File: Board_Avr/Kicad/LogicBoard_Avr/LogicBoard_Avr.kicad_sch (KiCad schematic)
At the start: 4 parts

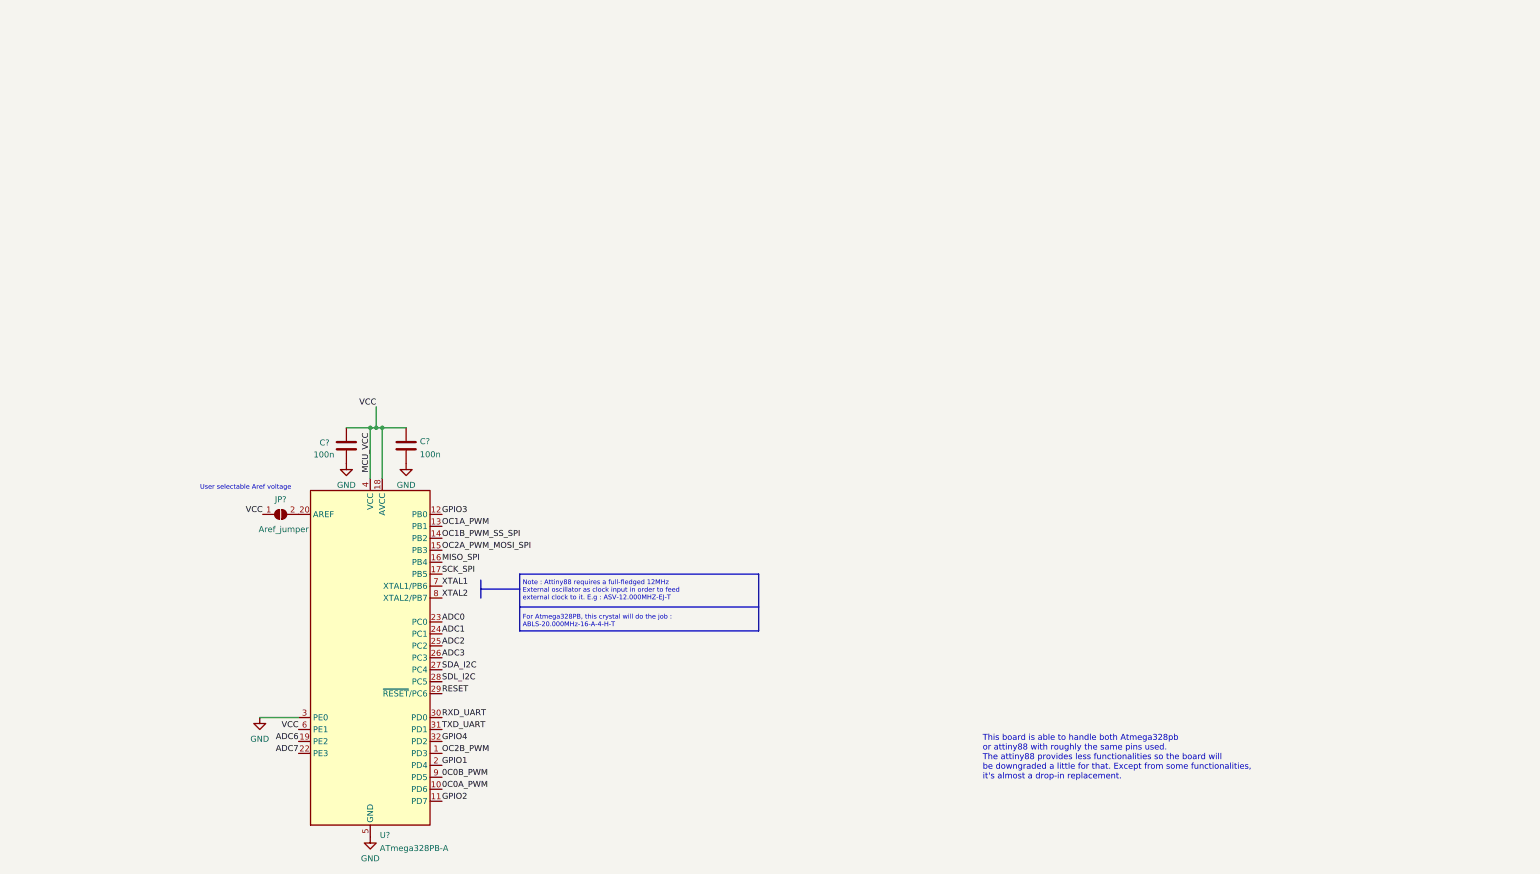
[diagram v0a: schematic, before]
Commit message: Added the Mechanical user interface hierarchical sheet and started schematics
Signed-off-by: bebenlebricolo <benoittarrade@hotmail.fr>
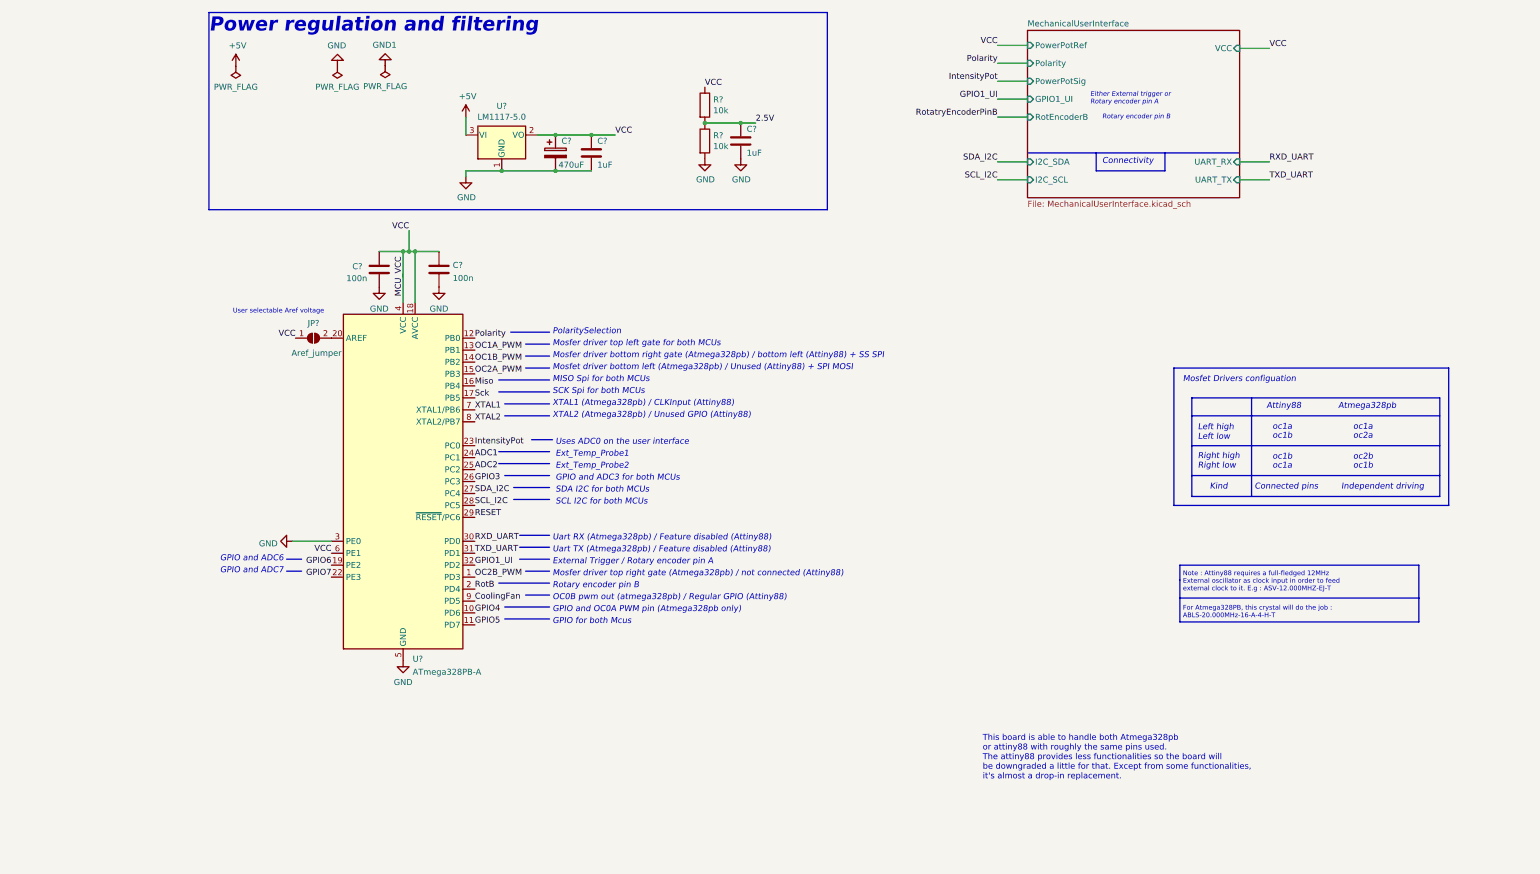
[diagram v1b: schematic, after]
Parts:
- added C? (x2): 1uF, Capacitor_SMD:C_1206_3216Metric_Pad1.33x1.80mm_HandSolder, symbol Device:C
- added C?: 470uF, Capacitor_SMD:CP_Elec_10x10, symbol Device:CP
- added R? (x2): 10k, Resistor_SMD:R_1206_3216Metric_Pad1.30x1.75mm_HandSolder, symbol Device:R
- added U?: LM1117-5.0, Package_TO_SOT_SMD:SOT-223-3_TabPin2, symbol Regulator_Linear:LM1117-5.0
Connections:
- net 0C0A_PWM is gone; now on net GPIO4: U?.10 (PD6)
- net ADC3 is gone; now on net GPIO3: U?.26 (PC3)
- net GND: now also C?.2, C?.2, C?.2, R?.2, U?.1 (GND)
- net GPIO3: no longer U?.12 (PB0)
- net GPIO4: no longer U?.32 (PD2)
- net MCU_VCC: now also C?.1, C?.1, R?.1, U?.2 (VO)
- net 0C0B_PWM renamed CoolingFan
- net ADC0 renamed IntensityPot
- net ADC6 renamed GPIO6
- net ADC7 renamed GPIO7
- net GPIO1 renamed RotB
- net GPIO2 renamed GPIO5
- net MISO_SPI renamed Miso
- net OC1B_PWM_SS_SPI renamed OC1B_PWM
- net OC2A_PWM_MOSI_SPI renamed OC2A_PWM
- net SCK_SPI renamed Sck
- net SDL_I2C renamed SCL_I2C
- new net +5V: U?.3 (VI)
- new net 2.5V: C?.1, R?.1, R?.2
- new net GPIO1_UI: U?.32 (PD2)
- new net Polarity: U?.12 (PB0)
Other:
- added sheet MechanicalUserInterface (MechanicalUserInterface.kicad_sch)
- note added: "Atmega328pb"
- note added: "Attiny88"
- note added: "Connected pins"
- note added: "Connectivity"
- note added: "Either External trigger or Rotary encoder pin A"
- note added: "Ext_Temp_Probe1"
- note added: "Ext_Temp_Probe2"
- note added: "External Trigger / Rotary encoder pin A"
- note added: "GPIO and ADC3 for both MCUs"
- note added: "GPIO and ADC6"
- note added: "GPIO and ADC7"
- note added: "GPIO and OC0A PWM pin (Atmega328pb only)"
- note added: "GPIO for both Mcus"
- note added: "Independent driving"
- note added: "Kind"
- note added: "Left high Left low Right high Right low"
- note added: "MISO Spi for both MCUs"
- note added: "Mosfer driver bottom right gate (Atmega328pb) / bottom left (Attiny88) + SS SPI"
- note added: "Mosfer driver top left gate for both MCUs"
- note added: "Mosfer driver top right gate (Atmega328pb) / not connected (Attiny88)"
- note added: "Mosfet Drivers configuation"
- note added: "Mosfet driver bottom left (Atmega328pb) / Unused (Attiny88) + SPI MOSI"
- note added: "OC0B pwm out (atmega328pb) / Regular GPIO (Attiny88)"
- note added: "PolaritySelection"
- note added: "Power regulation and filtering"
- note added: "Rotary encoder pin B"
- note added: "SCK Spi for both MCUs"
- note added: "SCL I2C for both MCUs"
- note added: "SDA I2C for both MCUs"
- note added: "Uart RX (Atmega328pb) / Feature disabled (Attiny88)"
- note added: "Uart TX (Atmega328pb) / Feature disabled (Attiny88)"
- note added: "Uses ADC0 on the user interface"
- note added: "XTAL1 (Atmega328pb) / CLKInput (Attiny88)"
- note added: "XTAL2 (Atmega328pb) / Unused GPIO (Attiny88)"
- note added: "oc1a"
- note added: "oc1b"
- note added: "oc2a"
- note added: "oc2b"
- moved on the sheet: C?, JP?, U?

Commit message: Designed basic layout for the mechanical user interface
Signed-off-by: bebenlebricolo <benoittarrade@hotmail.fr>
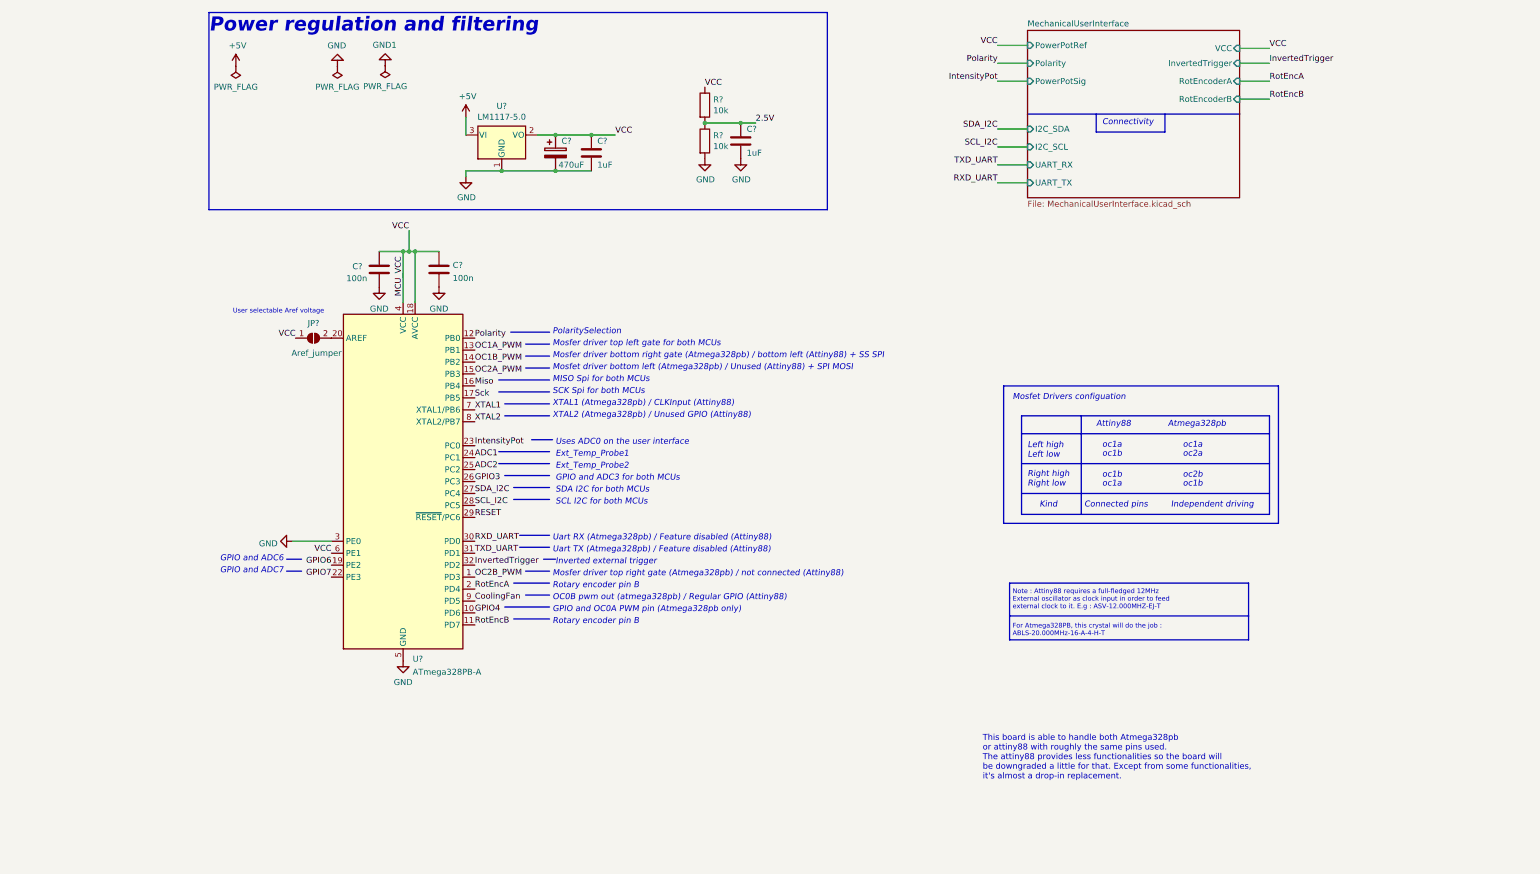
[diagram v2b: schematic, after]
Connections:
- net GPIO1_UI renamed InvertedTrigger
- net GPIO5 renamed RotEncB
- net RotB renamed RotEncA
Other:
- sheet MechanicalUserInterface ports: added InvertedTrigger, RotEncoderA; removed GPIO1_UI
- note added: "Inverted external trigger"
- note removed: "Either External trigger or Rotary encoder pin A"
- note removed: "External Trigger / Rotary encoder pin A"
- note removed: "GPIO for both Mcus"

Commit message: Added several other schematic sheets
Signed-off-by: bebenlebricolo <benoittarrade@hotmail.fr>
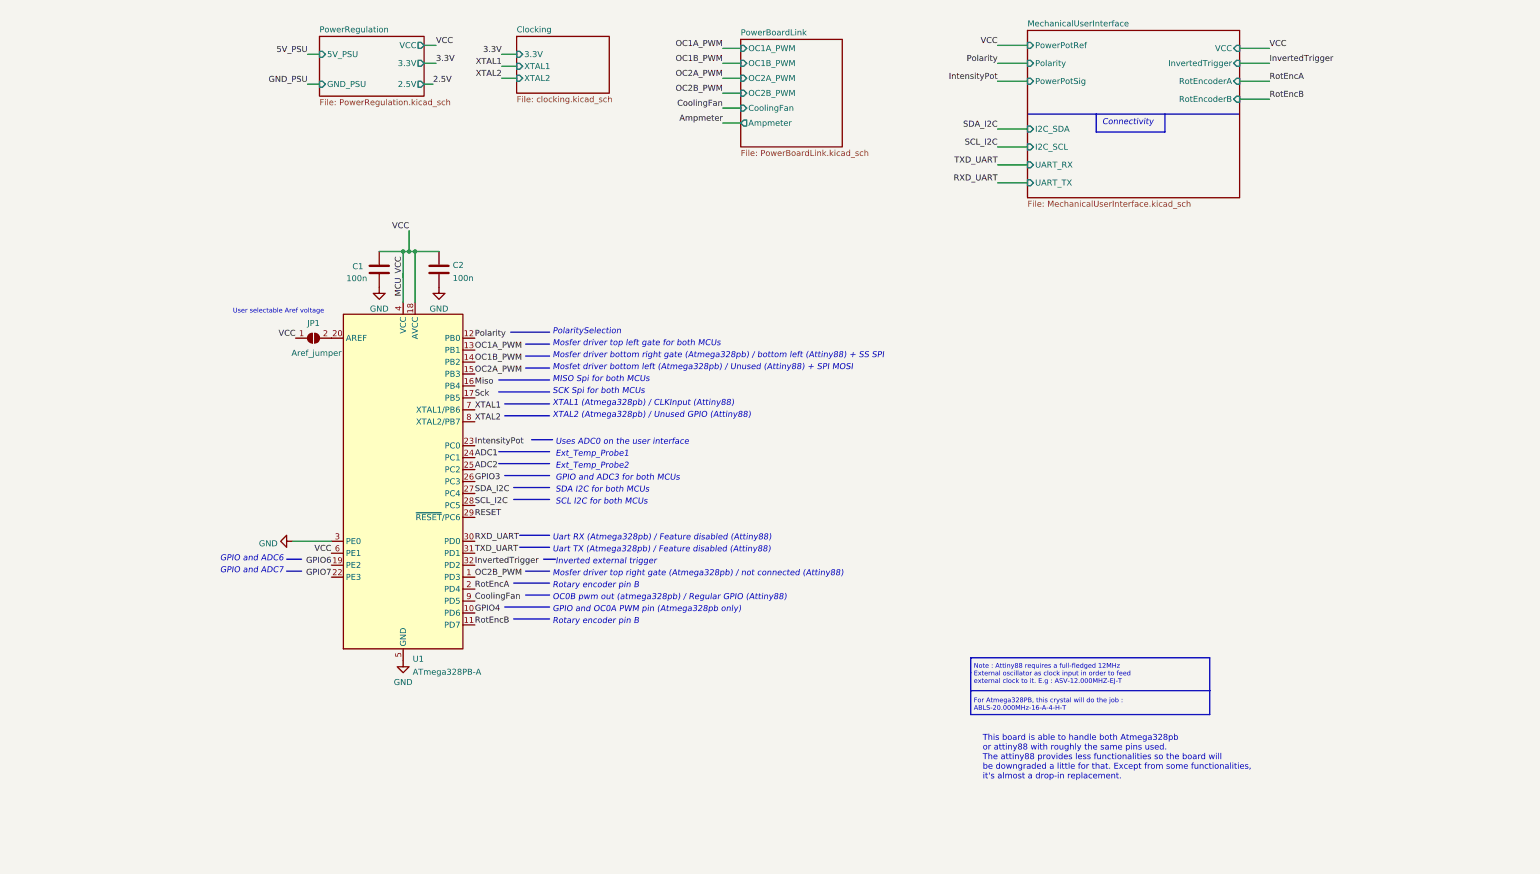
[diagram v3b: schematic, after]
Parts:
- removed C? (x2): 1uF, Capacitor_SMD:C_1206_3216Metric_Pad1.33x1.80mm_HandSolder, symbol Device:C
- removed C?: 470uF, Capacitor_SMD:CP_Elec_10x10, symbol Device:CP
- removed R? (x2): 10k, Resistor_SMD:R_1206_3216Metric_Pad1.30x1.75mm_HandSolder, symbol Device:R
- removed U?: LM1117-5.0, Package_TO_SOT_SMD:SOT-223-3_TabPin2, symbol Regulator_Linear:LM1117-5.0
- gave numbers to parts that had none: 4
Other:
- added sheet Clocking (clocking.kicad_sch)
- added sheet PowerBoardLink (PowerBoardLink.kicad_sch)
- added sheet PowerRegulation (PowerRegulation.kicad_sch)
- note removed: "Atmega328pb"
- note removed: "Attiny88"
- note removed: "Connected pins"
- note removed: "Independent driving"
- note removed: "Kind"
- note removed: "Left high Left low Right high Right low"
- note removed: "Mosfet Drivers configuation"
- note removed: "Power regulation and filtering"
- note removed: "oc1a"
- note removed: "oc1b"
- note removed: "oc2a"
- note removed: "oc2b"

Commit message: Added several external connections and reworked leds and output signals
Signed-off-by: bebenlebricolo <benoittarrade@hotmail.fr>
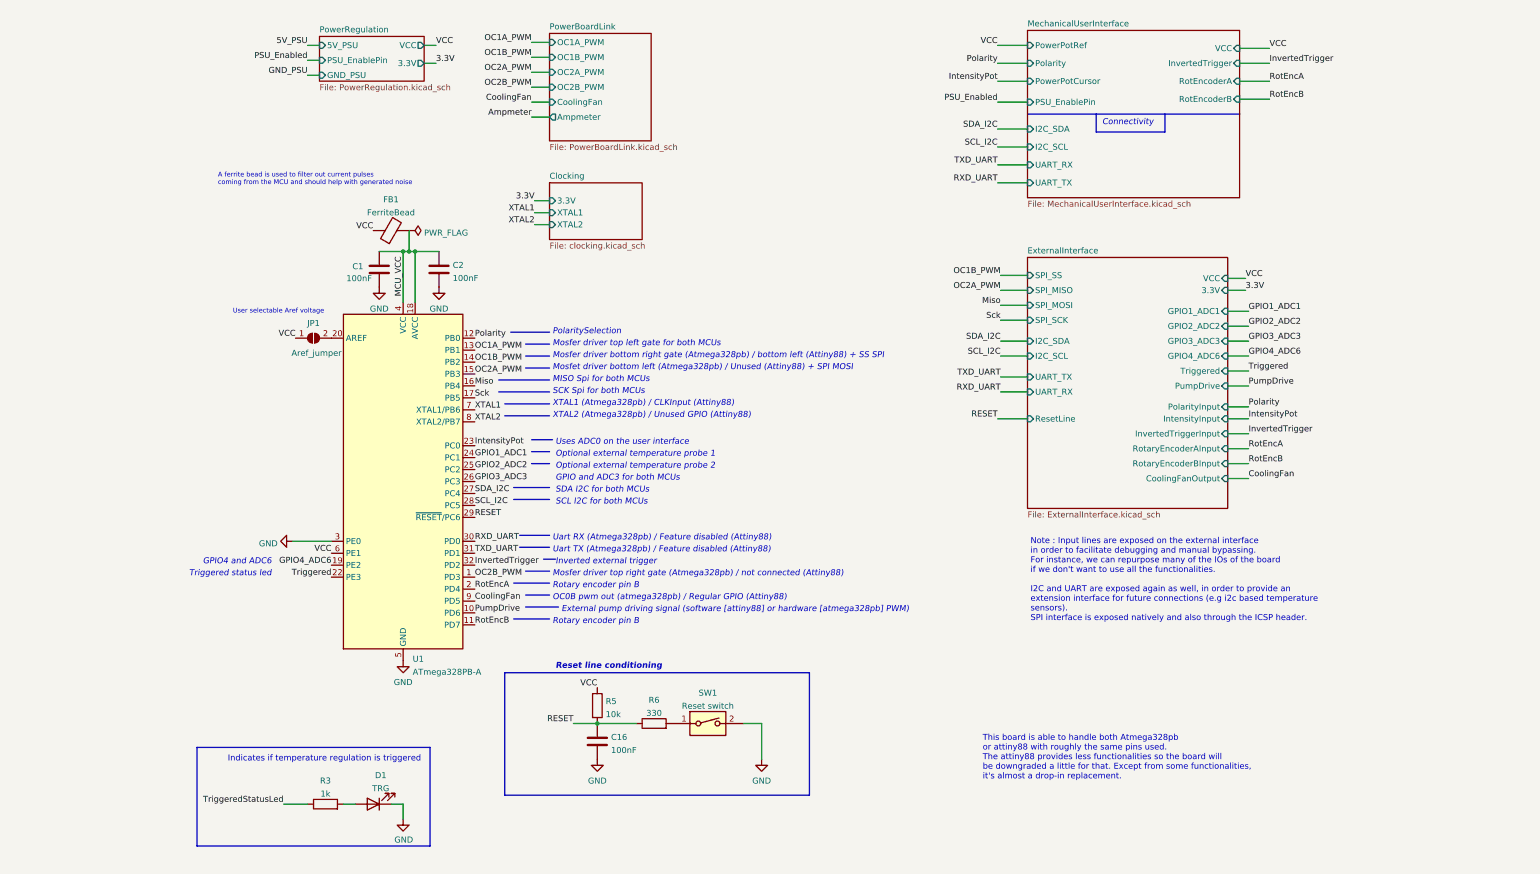
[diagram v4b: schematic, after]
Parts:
- added C16: 100nF, symbol Device:C
- added D1: TRG, symbol Device:LED
- added FB1: FerriteBead, symbol Device:FerriteBead
- added R3: 1k, symbol Device:R
- added R5: 10k, symbol Device:R
- added R6: 330, symbol Device:R
- added SW1: Reset switch, symbol Switch:SW_DIP_x01
- C1, C2: value 100n -> 100nF
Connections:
- net GND: now also C16.2, D1.1 (K), SW1.2
- net MCU_VCC: now also FB1.2; no longer JP1.1 (A), U1.6 (PE1)
- net RESET: now also C16.1, R5.2, R6.1
- net ADC1 renamed GPIO1_ADC1
- net ADC2 renamed GPIO2_ADC2
- net GPIO3 renamed GPIO3_ADC3
- net GPIO4 renamed PumpDrive
- net GPIO6 renamed GPIO4_ADC6
- net GPIO7 renamed Triggered
- new net: D1.2 (A), R3.2
- new net: R6.2, SW1.1
- new net TriggeredStatusLed: R3.1
- new net VCC: FB1.1, JP1.1 (A), R5.1, U1.6 (PE1)
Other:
- added sheet ExternalInterface (ExternalInterface.kicad_sch)
- sheet MechanicalUserInterface ports: added PSU_EnablePin, PowerPotCursor; removed PowerPotSig
- sheet PowerRegulation ports: added PSU_EnablePin; removed 2.5V
- note added: "A ferrite bead is used to filter out current pulses coming from the MCU and should help with generated noise"
- note added: "External pump driving signal (software [attiny88] or hardware [atmega328pb] PWM)"
- note added: "GPIO4 and ADC6"
- note added: "Indicates if temperature regulation is triggered"
- note added: "Note : Input lines are exposed on the external interface in order to facilitate debugging and manual bypassing. For instance, we can repurpose many of the IOs of the board if we don't want to use all the functionalities. I2C and UART are exposed again as well, in order to provide an extension interface for future connections (e.g i2c based temperature sensors). SPI interface is exposed natively a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"
- note added: "Optional external temperature probe 1"
- note added: "Optional external temperature probe 2"
- note added: "Reset line conditioning"
- note added: "Triggered status led"
- note removed: "Ext_Temp_Probe1"
- note removed: "Ext_Temp_Probe2"
- note removed: "For Atmega328PB, this crystal will do the job : ABLS-20.000MHz-16-A-4-H-T"
- note removed: "GPIO and ADC6"
- note removed: "GPIO and ADC7"
- note removed: "GPIO and OC0A PWM pin (Atmega328pb only)"
- note removed: "Note : Attiny88 requires a full-fledged 12MHz External oscillator as clock input in order to feed external clock to it. E.g : ASV-12.000MHZ-EJ-T"
